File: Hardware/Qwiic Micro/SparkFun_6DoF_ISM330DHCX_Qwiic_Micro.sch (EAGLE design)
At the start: 24 parts, among them J1 Qwiic Right Angle, U1 ISM330DHCX

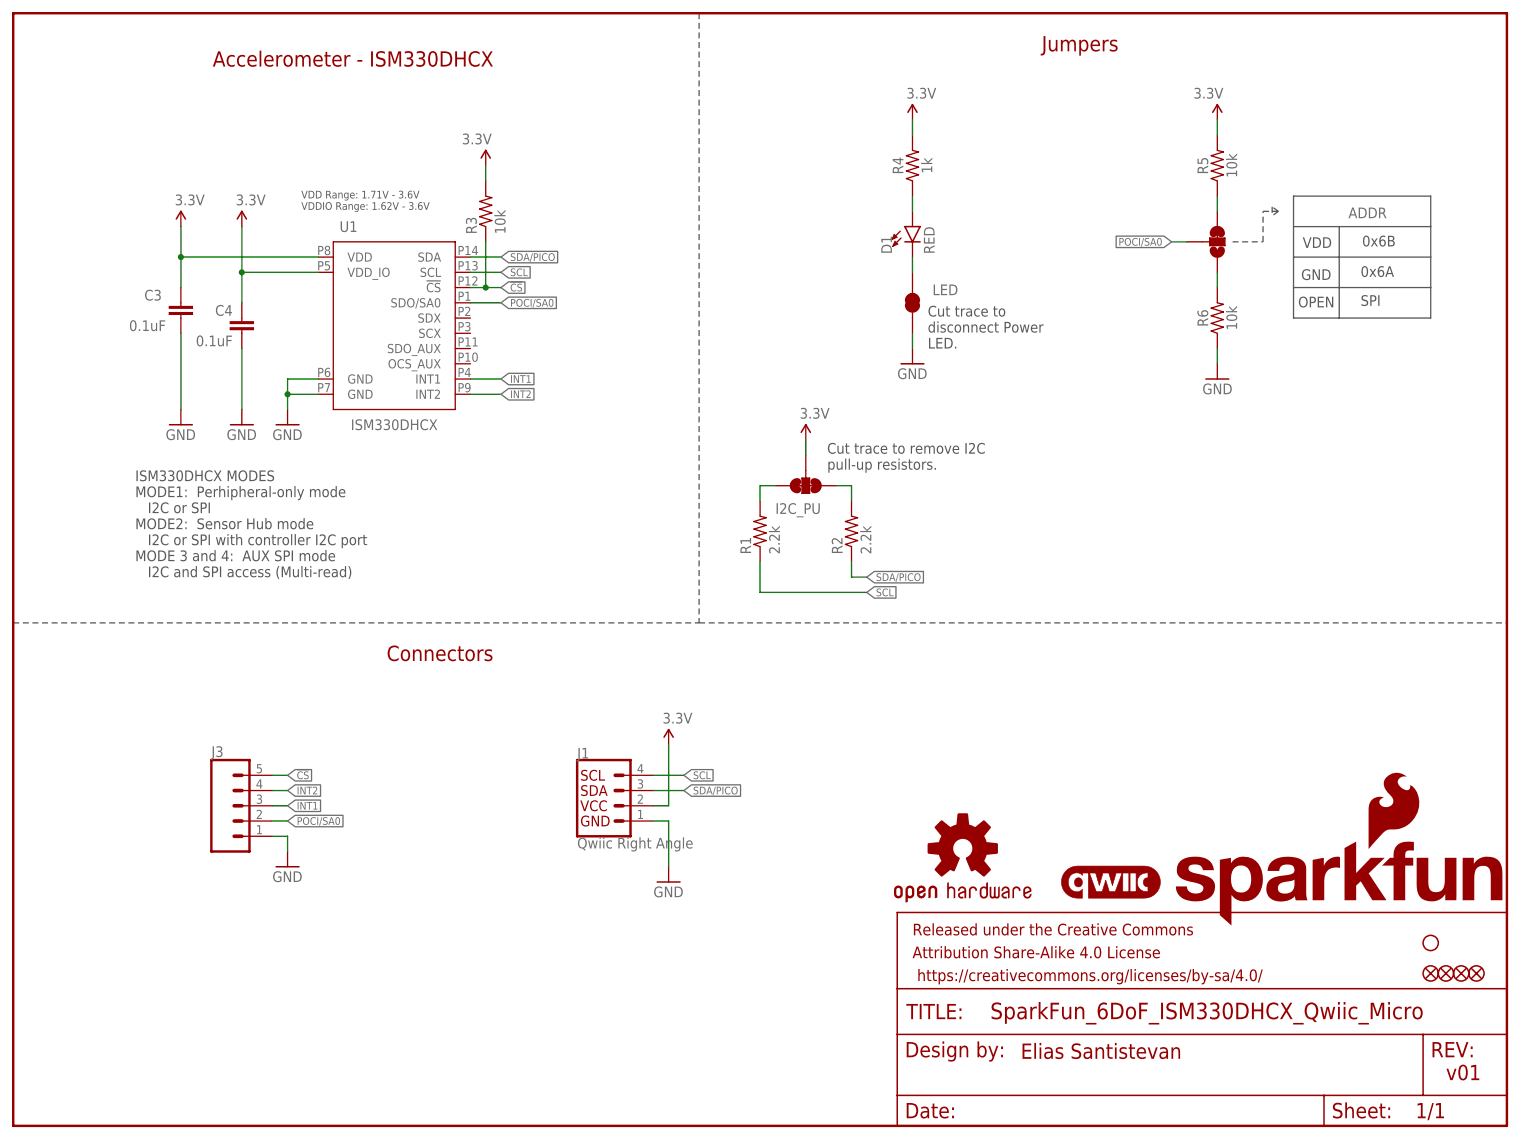
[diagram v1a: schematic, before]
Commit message: Resizes and reroutes the Qwiic Micro board
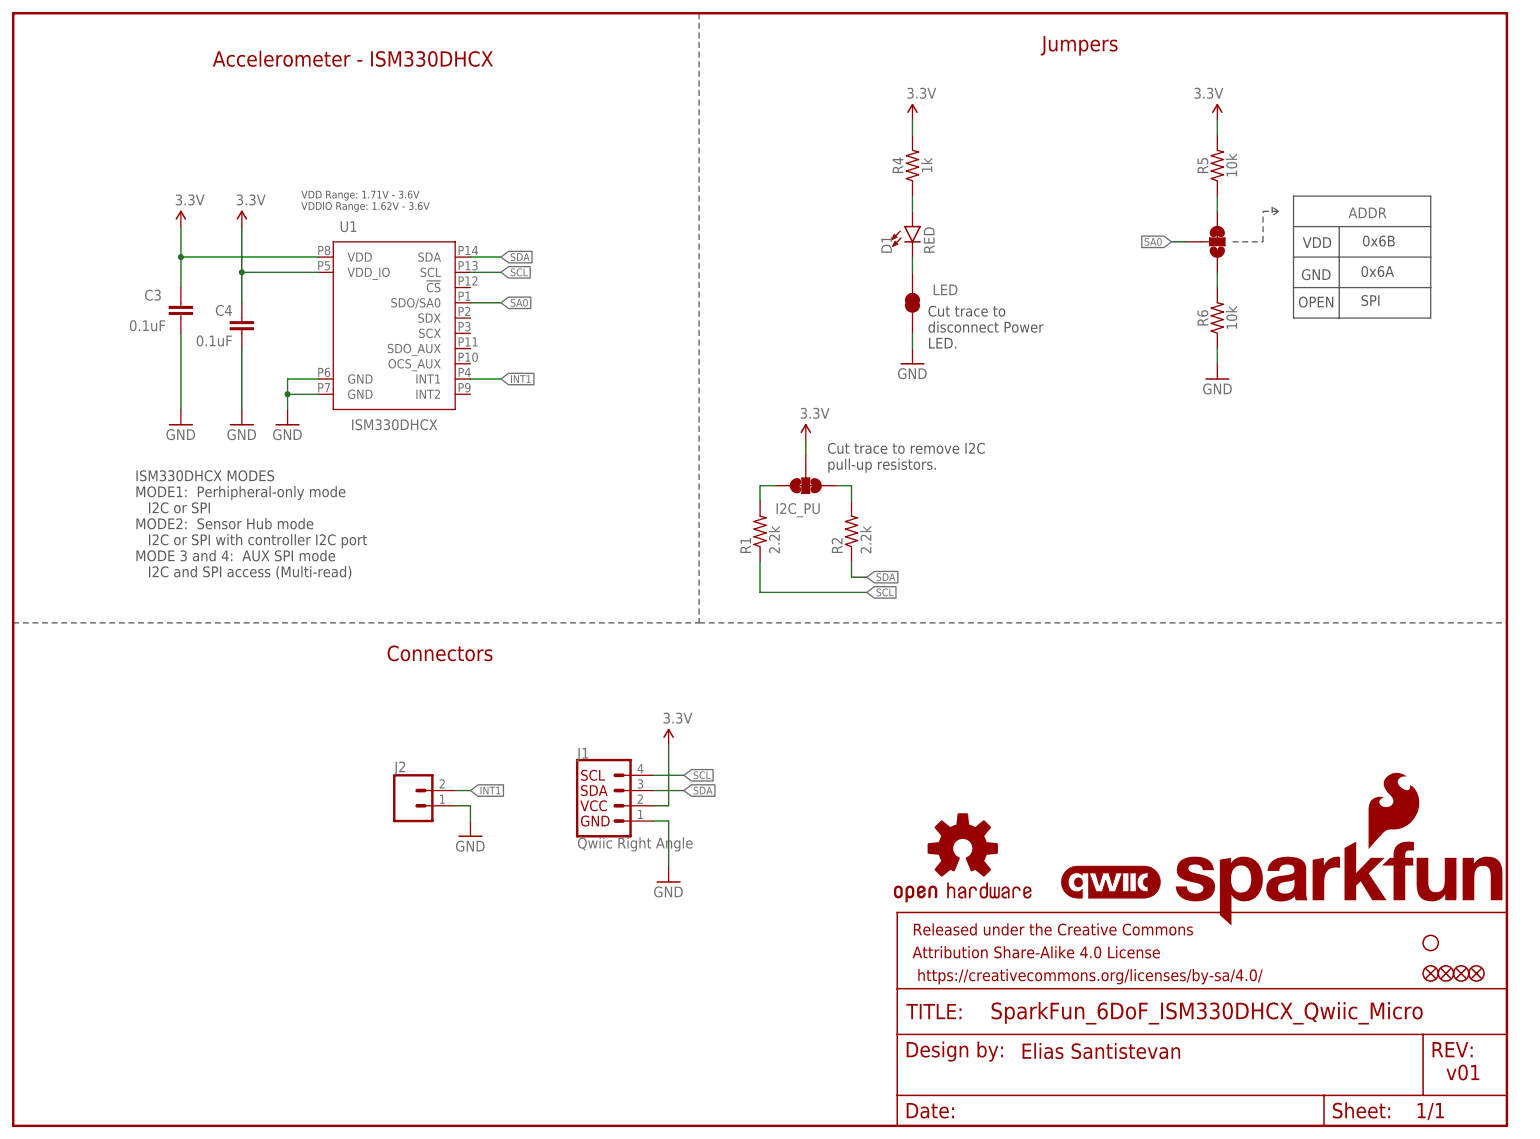
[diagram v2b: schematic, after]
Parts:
- removed J3: (no value), SparkFun-Connectors:CONN_05NO_SILK
- removed R3: 10k, SparkFun-Resistors:10KOHM-0402T-1/16W-1%
- added J2: (no value), SparkFun-Connectors:CONN_021X02_NO_SILK
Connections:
- net SDA/PICO renamed SDA
- removed net !CS!: J3.5, R3.1, U1.!CS!
- removed net INT2: J3.4, U1.INT2
- removed net POCI/SA0: ADDR.2, J3.2, U1.SDO/SA0
- new net SA0: ADDR.2, U1.SDO/SA0
- net 3.3V: no longer R3.2
- net GND: now also J2.1; no longer J3.1
- net INT1: now also J2.2; no longer J3.3
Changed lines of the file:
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@@
 <part name="GND6" library="SparkFun-PowerSymbols" deviceset="GND" device=""/>
 <part name="SUPPLY10" library="SparkFun-PowerSymbols" deviceset="3.3V" device=""/>
-<part name="SUPPLY11" library="SparkFun-PowerSymbols" deviceset="3.3V" device=""/>
 <part name="C4" library="SparkFun-Capacitors" deviceset="0.1UF" device="-0402T-6.3V-10%-X7R" value="0.1uF"/>
 <part name="GND10" library="SparkFun-PowerSymbols" deviceset="GND" device=""/>
@@
 <part name="FID1" library="SparkFun-Aesthetics" deviceset="FIDUCIAL" device="UFIDUCIAL" value="FIDUCIALUFIDUCIAL"/>
 <part name="FID2" library="SparkFun-Aesthetics" deviceset="FIDUCIAL" device="UFIDUCIAL" value="FIDUCIALUFIDUCIAL"/>
-<part name="R3" library="SparkFun-Resistors" deviceset="10KOHM" device="-0402T-1/16W-1%" value="10k"/>
 <part name="I2C_PU" library="SparkFun-Jumpers" deviceset="JUMPER-SMT_3_2-NC_TRACE" device="_SILK" package3d_urn="urn:adsk.eagle:package:39289/1" value="S_MODE"/>
 <part name="FD1" library="SparkFun-Aesthetics" deviceset="FIDUCIAL" device="UFIDUCIAL"/>
@@
 <part name="GND3" library="SparkFun-PowerSymbols" deviceset="GND" device=""/>
 <part name="SUPPLY1" library="SparkFun-PowerSymbols" deviceset="3.3V" device=""/>
-<part name="J3" library="SparkFun-Connectors" deviceset="CONN_05" device="NO_SILK"/>
-<part name="GND9" library="SparkFun-PowerSymbols" deviceset="GND" device=""/>
 <part name="LOGO1" library="SparkFun-Aesthetics" deviceset="QWIIC_LOGO" device="_3MM"/>
 <part name="LOGO3" library="SparkFun-Aesthetics" deviceset="SFE_LOGO_NAME_FLAME" device="BLANK"/>
+<part name="J2" library="SparkFun-Connectors" deviceset="CONN_02" device="1X02_NO_SILK"/>
+<part name="GND1" library="SparkFun-PowerSymbols" deviceset="GND" device=""/>
 </parts>
 <sheets>
@@
 <attribute name="VALUE" x="201.676" y="171.196" size="1.778" layer="96" font="vector" rot="MR0"/>
 </instance>
-<instance part="SUPPLY11" gate="G$1" x="78.74" y="160.02" smashed="yes" rot="MR0">
-<attribute name="VALUE" x="79.756" y="163.576" size="1.778" layer="96" font="vector" rot="MR0"/>
-</instance>
 <instance part="C4" gate="G$1" x="38.1" y="132.08" smashed="yes" rot="MR0">
 <attribute name="NAME" x="36.576" y="135.001" size="1.778" layer="95" font="vector" rot="MR0"/>
@@
 <instance part="FID1" gate="G$1" x="236.22" y="25.4" smashed="yes"/>
 <instance part="FID2" gate="G$1" x="238.76" y="25.4" smashed="yes"/>
-<instance part="R3" gate="G$1" x="78.74" y="152.4" smashed="yes" rot="R90">
-<attribute name="NAME" x="77.2414" y="148.59" size="1.778" layer="95" font="vector" rot="R90"/>
-<attribute name="VALUE" x="82.042" y="148.59" size="1.778" layer="96" font="vector" rot="R90"/>
-</instance>
 <instance part="I2C_PU" gate="G$1" x="132.08" y="106.68" smashed="yes" rot="MR270">
 <attribute name="NAME" x="127" y="103.759" size="1.778" layer="95" font="vector" rot="MR180"/>
@@
 <attribute name="VALUE" x="108.204" y="67.056" size="1.778" layer="96" font="vector"/>
 </instance>
-<instance part="J3" gate="G$1" x="35.56" y="53.34" smashed="yes">
-<attribute name="VALUE" x="33.02" y="43.434" size="1.778" layer="96" font="vector"/>
-<attribute name="NAME" x="33.02" y="61.468" size="1.778" layer="95" font="vector"/>
-</instance>
-<instance part="GND9" gate="1" x="45.72" y="43.18" smashed="yes">
-<attribute name="VALUE" x="43.18" y="40.64" size="1.778" layer="96" font="vector"/>
-</instance>
 <instance part="LOGO1" gate="G$1" x="182.88" y="40.64" smashed="yes"/>
 <instance part="LOGO3" gate="G$1" x="193.04" y="33.02" smashed="yes"/>
+<instance part="J2" gate="G$1" x="66.04" y="53.34" smashed="yes">
+<attribute name="VALUE" x="63.5" y="48.514" size="1.778" layer="96" font="vector"/>
+<attribute name="NAME" x="63.5" y="58.928" size="1.778" layer="95" font="vector"/>
+</instance>
+<instance part="GND1" gate="1" x="76.2" y="48.26" smashed="yes">
+<attribute name="VALUE" x="73.66" y="45.72" size="1.778" layer="96" font="vector"/>
+</instance>
 </instances>
 <busses>
@@
 </segment>
 <segment>
-<wire x1="43.18" y1="48.26" x2="45.72" y2="48.26" width="0.1524" layer="91"/>
-<wire x1="45.72" y1="48.26" x2="45.72" y2="45.72" width="0.1524" layer="91"/>
-<pinref part="GND9" gate="1" pin="GND"/>
-<pinref part="J3" gate="G$1" pin="1"/>
+<pinref part="J2" gate="G$1" pin="1"/>
+<wire x1="73.66" y1="53.34" x2="76.2" y2="53.34" width="0.1524" layer="91"/>
+<wire x1="76.2" y1="53.34" x2="76.2" y2="50.8" width="0.1524" layer="91"/>
+<pinref part="GND1" gate="1" pin="GND"/>
 </segment>
 </net>
@@
 </segment>
 </net>
-<net name="SDA/PICO" class="0">
+<net name="SDA" class="0">
 <segment>
 <wire x1="76.2" y1="144.78" x2="81.28" y2="144.78" width="0.1524" layer="91"/>
@@
 </segment>
 </net>
-<net name="!CS!" class="0">
-<segment>
-<wire x1="76.2" y1="139.7" x2="78.74" y2="139.7" width="0.1524" layer="91"/>
-<wire x1="78.74" y1="139.7" x2="78.74" y2="147.32" width="0.1524" layer="91"/>
-<pinref part="R3" gate="G$1" pin="1"/>
-<label x="81.28" y="139.7" size="1.27" layer="95" font="vector" xref="yes"/>
-<wire x1="81.28" y1="139.7" x2="78.74" y2="139.7" width="0.1524" layer="91"/>
-<junction x="78.74" y="139.7"/>
-<pinref part="U1" gate="G$1" pin="!CS!"/>
-</segment>
-<segment>
-<wire x1="43.18" y1="58.42" x2="45.72" y2="58.42" width="0.1524" layer="91"/>
-<label x="45.72" y="58.42" size="1.27" layer="95" font="vector" xref="yes"/>
-<pinref part="J3" gate="G$1" pin="5"/>
-</segment>
-</net>
-<net name="POCI/SA0" class="0">
+<net name="SA0" class="0">
 <segment>
 <wire x1="76.2" y1="137.16" x2="81.28" y2="137.16" width="0.1524" layer="91"/>
@@
 <label x="193.04" y="147.32" size="1.27" layer="95" font="vector" rot="R180" xref="yes"/>
 </segment>
-<segment>
-<wire x1="43.18" y1="50.8" x2="45.72" y2="50.8" width="0.1524" layer="91"/>
-<label x="45.72" y="50.8" size="1.27" layer="95" font="vector" xref="yes"/>
-<pinref part="J3" gate="G$1" pin="2"/>
-</segment>
 </net>
 <net name="INT1" class="0">
@@
 </segment>
 <segment>
-<wire x1="43.18" y1="53.34" x2="45.72" y2="53.34" width="0.1524" layer="91"/>
-<label x="45.72" y="53.34" size="1.27" layer="95" font="vector" xref="yes"/>
-<pinref part="J3" gate="G$1" pin="3"/>
-</segment>
-</net>
-<net name="INT2" class="0">
-<segment>
-<wire x1="76.2" y1="121.92" x2="81.28" y2="121.92" width="0.1524" layer="91"/>
-<label x="81.28" y="121.92" size="1.27" layer="95" font="vector" xref="yes"/>
-<pinref part="U1" gate="G$1" pin="INT2"/>
-</segment>
-<segment>
-<wire x1="43.18" y1="55.88" x2="45.72" y2="55.88" width="0.1524" layer="91"/>
-<label x="45.72" y="55.88" size="1.27" layer="95" font="vector" xref="yes"/>
-<pinref part="J3" gate="G$1" pin="4"/>
+<wire x1="73.66" y1="55.88" x2="76.2" y2="55.88" width="0.1524" layer="91"/>
+<label x="76.2" y="55.88" size="1.27" layer="95" font="vector" xref="yes"/>
+<pinref part="J2" gate="G$1" pin="2"/>
 </segment>
 </net>
@@
 </segment>
 <segment>
-<pinref part="SUPPLY11" gate="G$1" pin="3.3V"/>
-<pinref part="R3" gate="G$1" pin="2"/>
-<wire x1="78.74" y1="160.02" x2="78.74" y2="157.48" width="0.1524" layer="91"/>
-</segment>
-<segment>
